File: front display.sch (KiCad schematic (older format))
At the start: 2 parts, among them P1 CONN_02X14

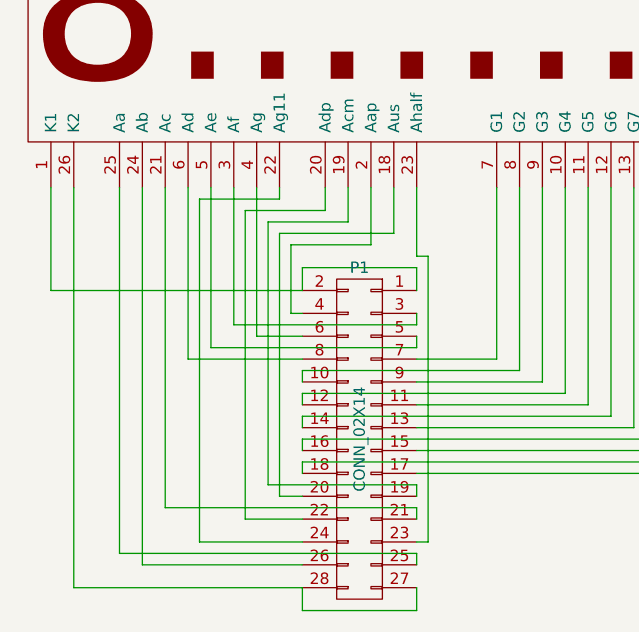
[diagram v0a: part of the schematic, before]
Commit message: Sch changes.
Changing wire positions and changing kathode wires to labels.
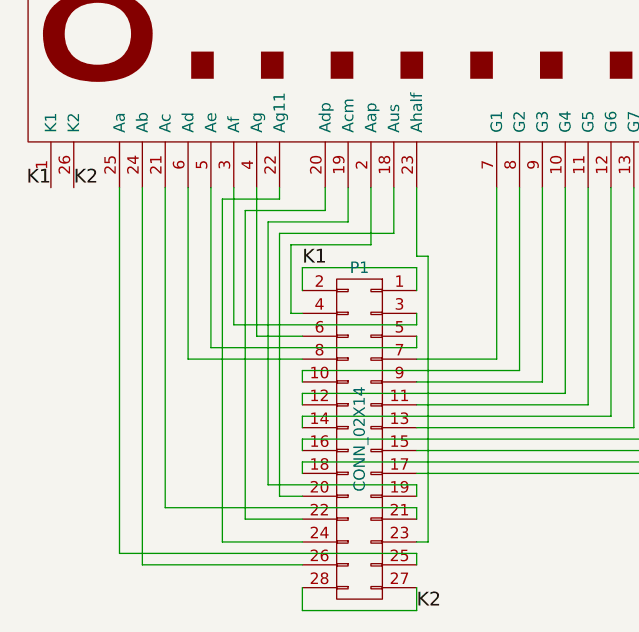
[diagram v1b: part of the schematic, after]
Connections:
- net K1: now reaches DISP1.1 (K1), P1.1 (P1), P1.2 (P2)
- net K2: now reaches DISP1.26 (K2), P1.27 (P27), P1.28 (P28)
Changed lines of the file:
@@
 $EndComp
-Wire Wire Line
-	3100 4550 3100 4100
 Wire Wire Line
 	4700 5850 4700 5950
@@
 	4200 5950 4200 5850
 Wire Wire Line
-	4200 5850 3200 5850
-Wire Wire Line
-	3200 5850 3200 4100
-Wire Wire Line
 	4700 4550 4700 4450
 Wire Wire Line
@@
 Wire Wire Line
 	4200 4450 4200 4550
-Wire Wire Line
-	4200 4550 3100 4550
 Wire Wire Line
 	4200 4650 4150 4650
@@
 	4100 4100 4100 4150
 Wire Wire Line
-	4100 4150 3750 4150
+	4100 4150 3850 4150
 Wire Wire Line
-	3750 4150 3750 5650
+	3850 4150 3850 5650
 Wire Wire Line
-	3750 5650 4200 5650
+	3850 5650 4200 5650
 Wire Wire Line
 	4700 5650 4750 5650
@@
 Wire Wire Line
 	3400 5700 3400 4100
+Text Label 4200 4450 0    60   ~ 0
+K1
+Text Label 4700 5950 0    60   ~ 0
+K2
+Text Label 3100 4100 2    60   ~ 0
+K1
+Text Label 3200 4100 0    60   ~ 0
+K2
 $EndSCHEMATC
